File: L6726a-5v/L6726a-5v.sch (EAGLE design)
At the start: 32 parts, among them IC1 L6727A, U1 5V

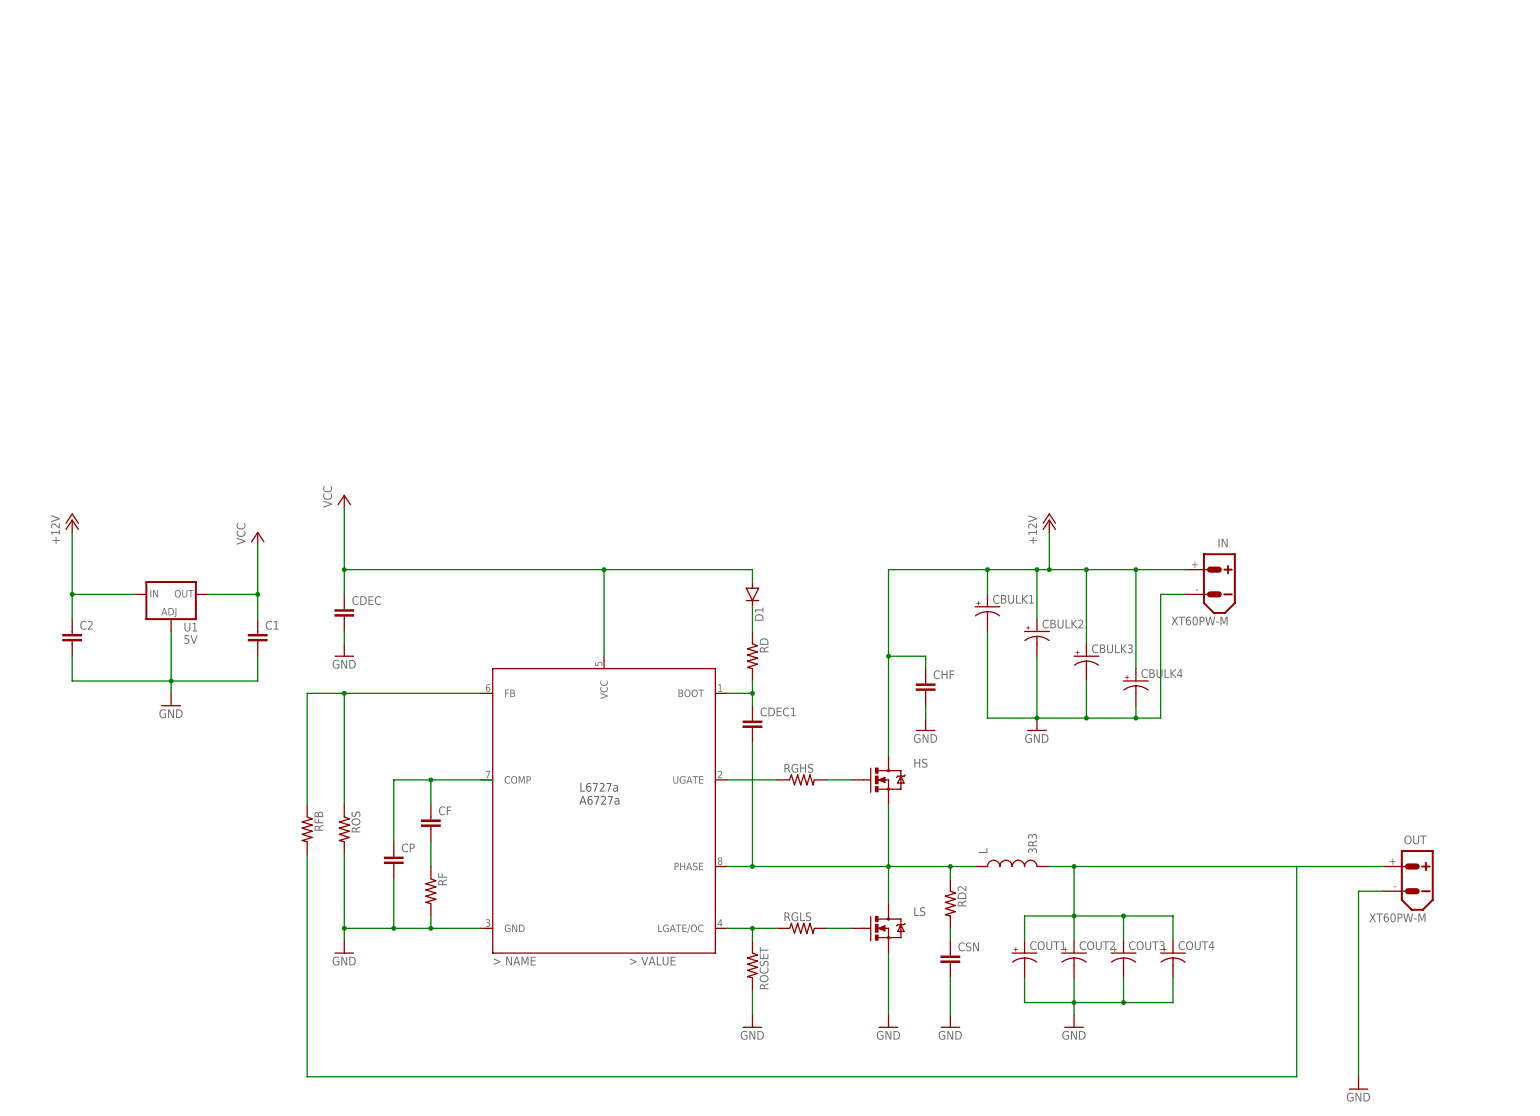
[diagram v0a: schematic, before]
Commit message: renamed files and folders, layout mostly complete
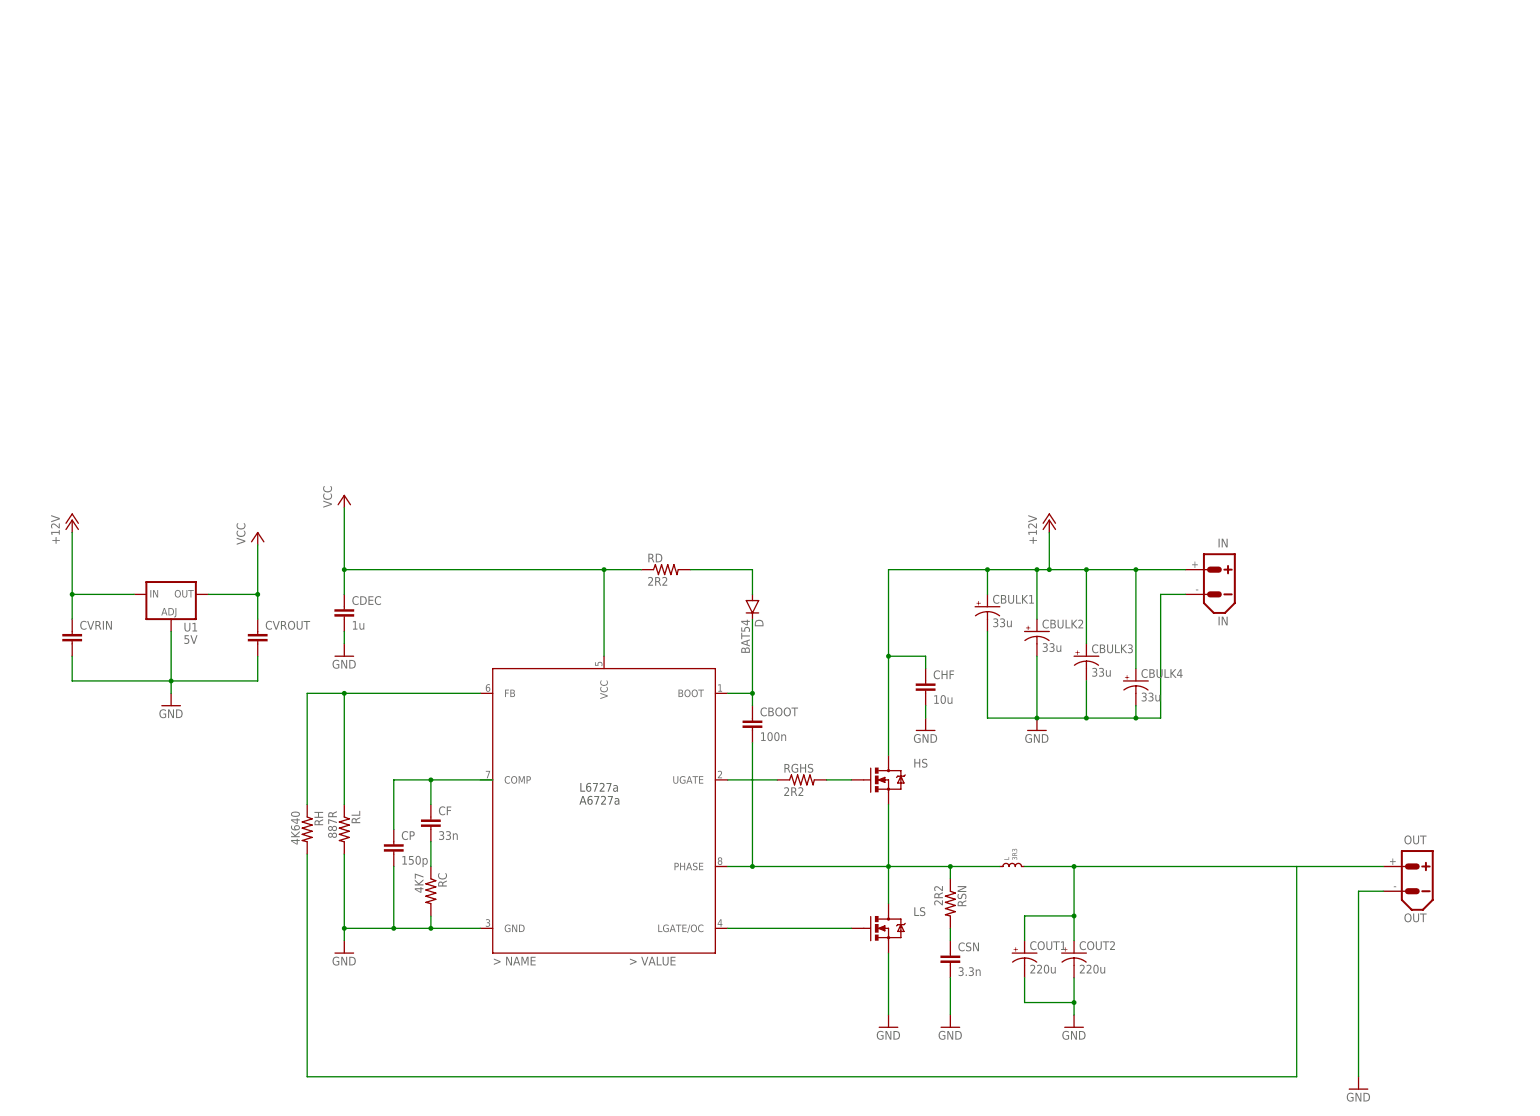
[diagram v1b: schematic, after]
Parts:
- removed CDEC1: (no value), rcl:C-EUC1206
- removed COUT3, COUT4: (no value), rcl:CPOL-USSANYO_SMD_E7
- removed D1: (no value), SparkFun-DiscreteSemi:DIODESOD123
- removed RGLS, ROCSET: (no value), rcl:R-US_R0603
- added CBOOT: 100n, rcl:C-EUC0805
- added D: BAT54, SparkFun-DiscreteSemi:DIODESOD123
- CBULK1, CBULK2, CBULK3, CBULK4: value (none) -> 33u
- CDEC: value (none) -> 1u; device rcl:C-EUC1206 -> rcl:C-EUC0603
- CF: value (none) -> 33n; device rcl:C-EUC1206 -> rcl:C-EUC0603
- CHF: value (none) -> 10u
- COUT1, COUT2: value (none) -> 220u
- CP: value (none) -> 150p; device rcl:C-EUC1206 -> rcl:C-EUC0603
- CSN: value (none) -> 3.3n; device rcl:C-EUC1206 -> rcl:C-EUC0603
- IN: value XT60PW-M -> IN
- L: device SparkFun-Passives:INDUCTORSDR13-7-270ML -> coilcraft:INDUCTOR.XAL1010
- OUT: value XT60PW-M -> OUT
- RC: value (none) -> 4K7
- RD, RGHS, RSN: value (none) -> 2R2
- RH: value (none) -> 4K640
- RL: value (none) -> 887R
- renumbered C1 to CVROUT, C2 to CVRIN, RD2 to RSN, RF to RC, RFB to RH, ROS to RL
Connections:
- removed net LGATE`: IC1.LGATE/OC, RGLS.1, ROCSET.1
- removed net N$2: CDEC1.1, IC1.BOOT, RD.2
- new net BOOT: CBOOT.1, D.C, IC1.BOOT
- net GND: no longer COUT3.-, COUT4.-, ROCSET.2
- net LGATE: now also IC1.LGATE/OC; no longer RGLS.2
- net N$1: now also D.A, RD.2; no longer D1.C, RD.1
- net PHASE: now also CBOOT.2; no longer CDEC1.2
- net VCC: now also RD.1; no longer D1.A
- net VOUT: no longer COUT3.+, COUT4.+
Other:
- moved on the sheet: CP, RD

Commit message: lots of progress with routing, verifying component packages
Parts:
- CBULK1, CBULK2, CBULK3, CBULK4: device rcl:CPOL-USSANYO_SMD_E7 -> rcl:C-EUC2220K
- COUT1, COUT2: value 220u -> 330u; device rcl:CPOL-USSANYO_SMD_E7 -> rcl:CPOL-USSANYO_SMD_C6
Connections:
- net +12V: now also CBULK1.1, CBULK2.1, CBULK3.1, CBULK4.1; no longer CBULK1.+, CBULK2.+, CBULK3.+, CBULK4.+
- net GND: now also CBULK1.2, CBULK2.2, CBULK3.2, CBULK4.2; no longer CBULK1.-, CBULK2.-, CBULK3.-, CBULK4.-
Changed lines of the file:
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@@
 <layer number="23" name="tOrigins" color="15" fill="1" visible="yes" active="no"/>
 <layer number="24" name="bOrigins" color="15" fill="1" visible="yes" active="no"/>
-<layer number="25" name="tNames" color="6" fill="1" visible="yes" active="no"/>
+<layer number="25" name="tNames" color="14" fill="1" visible="yes" active="no"/>
 <layer number="26" name="bNames" color="13" fill="1" visible="yes" active="no"/>
-<layer number="27" name="tValues" color="7" fill="1" visible="yes" active="no"/>
-<layer number="28" name="bValues" color="7" fill="1" visible="yes" active="no"/>
+<layer number="27" name="tValues" color="6" fill="1" visible="yes" active="no"/>
+<layer number="28" name="bValues" color="5" fill="1" visible="yes" active="no"/>
 <layer number="29" name="tStop" color="7" fill="3" visible="no" active="no"/>
 <layer number="30" name="bStop" color="7" fill="6" visible="no" active="no"/>
@@
 <part name="CSN" library="rcl" deviceset="C-EU" device="C0603" value="3.3n"/>
 <part name="RSN" library="rcl" deviceset="R-US_" device="R0603" value="2R2"/>
-<part name="CBULK1" library="rcl" deviceset="CPOL-US" device="SANYO_SMD_E7" value="33u"/>
-<part name="COUT1" library="rcl" deviceset="CPOL-US" device="SANYO_SMD_E7" value="220u"/>
-<part name="CBULK2" library="rcl" deviceset="CPOL-US" device="SANYO_SMD_E7" value="33u"/>
+<part name="COUT1" library="rcl" deviceset="CPOL-US" device="SANYO_SMD_C6" value="330u"/>
 <part name="GND8" library="supply1" deviceset="GND" device=""/>
-<part name="COUT2" library="rcl" deviceset="CPOL-US" device="SANYO_SMD_E7" value="220u"/>
+<part name="COUT2" library="rcl" deviceset="CPOL-US" device="SANYO_SMD_C6" value="330u"/>
 <part name="GND10" library="supply1" deviceset="GND" device=""/>
 <part name="GND4" library="supply1" deviceset="GND" device=""/>
@@
 <part name="OUT" library="amass" deviceset="XT60" device="PW-M" value="OUT"/>
 <part name="IN" library="amass" deviceset="XT60" device="PW-M" value="IN"/>
-<part name="CBULK3" library="rcl" deviceset="CPOL-US" device="SANYO_SMD_E7" value="33u"/>
-<part name="CBULK4" library="rcl" deviceset="CPOL-US" device="SANYO_SMD_E7" value="33u"/>
 <part name="L" library="coilcraft" deviceset="INDUCTOR" device=".XAL1010" value="3R3"/>
+<part name="CBULK1" library="rcl" deviceset="C-EU" device="C2220K" value="33u"/>
+<part name="CBULK2" library="rcl" deviceset="C-EU" device="C2220K" value="33u"/>
+<part name="CBULK3" library="rcl" deviceset="C-EU" device="C2220K" value="33u"/>
+<part name="CBULK4" library="rcl" deviceset="C-EU" device="C2220K" value="33u"/>
 </parts>
 <sheets>
@@
 <instance part="CSN" gate="G$1" x="149.86" y="10.16"/>
 <instance part="RSN" gate="G$1" x="149.86" y="20.32" rot="R270"/>
-<instance part="CBULK1" gate="G$1" x="157.48" y="81.28"/>
 <instance part="COUT1" gate="G$1" x="165.1" y="10.16"/>
-<instance part="CBULK2" gate="G$1" x="167.64" y="76.2"/>
 <instance part="GND8" gate="1" x="167.64" y="55.88"/>
 <instance part="COUT2" gate="G$1" x="175.26" y="10.16"/>
@@
 <instance part="OUT" gate="G$1" x="243.84" y="25.4" rot="MR0"/>
 <instance part="IN" gate="G$1" x="203.2" y="86.36" rot="MR0"/>
+<instance part="L" gate="G$1" x="162.56" y="27.94"/>
+<instance part="CBULK1" gate="G$1" x="157.48" y="81.28"/>
+<instance part="CBULK2" gate="G$1" x="167.64" y="76.2"/>
 <instance part="CBULK3" gate="G$1" x="177.8" y="71.12"/>
 <instance part="CBULK4" gate="G$1" x="187.96" y="66.04"/>
-<instance part="L" gate="G$1" x="162.56" y="27.94"/>
 </instances>
 <busses>
@@
 <wire x1="157.48" y1="83.82" x2="157.48" y2="88.9" width="0.1524" layer="91"/>
 <junction x="157.48" y="88.9"/>
-<pinref part="CBULK1" gate="G$1" pin="+"/>
-<pinref part="CBULK2" gate="G$1" pin="+"/>
 <wire x1="167.64" y1="88.9" x2="167.64" y2="78.74" width="0.1524" layer="91"/>
 <junction x="167.64" y="88.9"/>
@@
 <wire x1="198.12" y1="88.9" x2="187.96" y2="88.9" width="0.1524" layer="91"/>
 <junction x="177.8" y="88.9"/>
-<pinref part="CBULK3" gate="G$1" pin="+"/>
-<pinref part="CBULK4" gate="G$1" pin="+"/>
 <wire x1="187.96" y1="88.9" x2="177.8" y2="88.9" width="0.1524" layer="91"/>
 <wire x1="187.96" y1="68.58" x2="187.96" y2="88.9" width="0.1524" layer="91"/>
 <junction x="187.96" y="88.9"/>
+<pinref part="CBULK1" gate="G$1" pin="1"/>
+<pinref part="CBULK2" gate="G$1" pin="1"/>
+<pinref part="CBULK3" gate="G$1" pin="1"/>
+<pinref part="CBULK4" gate="G$1" pin="1"/>
 </segment>
 </net>
@@
 <segment>
 <pinref part="GND8" gate="1" pin="GND"/>
-<pinref part="CBULK2" gate="G$1" pin="-"/>
 <wire x1="167.64" y1="58.42" x2="167.64" y2="71.12" width="0.1524" layer="91"/>
 <wire x1="157.48" y1="58.42" x2="157.48" y2="76.2" width="0.1524" layer="91"/>
-<pinref part="CBULK1" gate="G$1" pin="-"/>
 <wire x1="157.48" y1="58.42" x2="167.64" y2="58.42" width="0.1524" layer="91"/>
 <junction x="167.64" y="58.42"/>
@@
 <wire x1="193.04" y1="58.42" x2="187.96" y2="58.42" width="0.1524" layer="91"/>
 <junction x="177.8" y="58.42"/>
-<pinref part="CBULK3" gate="G$1" pin="-"/>
-<pinref part="CBULK4" gate="G$1" pin="-"/>
 <wire x1="187.96" y1="58.42" x2="177.8" y2="58.42" width="0.1524" layer="91"/>
 <wire x1="187.96" y1="58.42" x2="187.96" y2="60.96" width="0.1524" layer="91"/>
 <junction x="187.96" y="58.42"/>
-</segment>
-<segment>
+<pinref part="CBULK1" gate="G$1" pin="2"/>
+<pinref part="CBULK2" gate="G$1" pin="2"/>
+<pinref part="CBULK3" gate="G$1" pin="2"/>
+<pinref part="CBULK4" gate="G$1" pin="2"/>
+</segment>
+<segment>

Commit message: changed mosfet package, blew up layout
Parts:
- CF: value 33n -> 15n
- CP: value 150p -> 22p
- HS, LS: value MOSFET-NCHANNELFDS6630A -> N_MOSFET_POWERSO8; device SparkFun-DiscreteSemi:MOSFET-NCHANNELFDS6630A -> power-mosfet:N_MOSFET_POWERSO8
- RC: value 4K7 -> 18K0
- RH, RL: device rcl:R-US_R0603 -> rcl:R-US_R0805
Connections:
- net N$3 renamed CC
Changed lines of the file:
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@@
 <part name="RGHS" library="rcl" deviceset="R-US_" device="R0603" value="2R2"/>
 <part name="CHF" library="rcl" deviceset="C-EU" device="C1206" value="10u"/>
-<part name="HS" library="SparkFun-DiscreteSemi" deviceset="MOSFET-NCHANNEL" device="FDS6630A" value=""/>
 <part name="P+4" library="supply1" deviceset="+12V" device=""/>
 <part name="GND3" library="supply1" deviceset="GND" device=""/>
-<part name="LS" library="SparkFun-DiscreteSemi" deviceset="MOSFET-NCHANNEL" device="FDS6630A" value=""/>
 <part name="GND5" library="supply1" deviceset="GND" device=""/>
 <part name="GND7" library="supply1" deviceset="GND" device=""/>
@@
 <part name="GND10" library="supply1" deviceset="GND" device=""/>
 <part name="GND4" library="supply1" deviceset="GND" device=""/>
-<part name="RH" library="rcl" deviceset="R-US_" device="R0603" value="4K640"/>
-<part name="RL" library="rcl" deviceset="R-US_" device="R0603" value="887R"/>
-<part name="CP" library="rcl" deviceset="C-EU" device="C0603" value="150p"/>
-<part name="CF" library="rcl" deviceset="C-EU" device="C0603" value="33n"/>
-<part name="RC" library="rcl" deviceset="R-US_" device="R0603" value="4K7"/>
+<part name="RH" library="rcl" deviceset="R-US_" device="R0805" value="4K640"/>
+<part name="RL" library="rcl" deviceset="R-US_" device="R0805" value="887R"/>
+<part name="CP" library="rcl" deviceset="C-EU" device="C0603" value="22p"/>
+<part name="CF" library="rcl" deviceset="C-EU" device="C0603" value="15n"/>
+<part name="RC" library="rcl" deviceset="R-US_" device="R0603" value="18K0"/>
 <part name="GND9" library="supply1" deviceset="GND" device=""/>
 <part name="OUT" library="amass" deviceset="XT60" device="PW-M" value="OUT"/>
@@
 <part name="CBULK3" library="rcl" deviceset="C-EU" device="C2220K" value="33u"/>
 <part name="CBULK4" library="rcl" deviceset="C-EU" device="C2220K" value="33u"/>
+<part name="HS" library="power-mosfet" deviceset="N_MOSFET_POWERSO8" device="" value=""/>
+<part name="LS" library="power-mosfet" deviceset="N_MOSFET_POWERSO8" device="" value=""/>
 </parts>
 <sheets>
@@
 <instance part="RGHS" gate="G$1" x="119.38" y="45.72"/>
 <instance part="CHF" gate="G$1" x="144.78" y="66.04"/>
-<instance part="HS" gate="G$1" x="137.16" y="45.72"/>
 <instance part="P+4" gate="1" x="170.18" y="99.06"/>
 <instance part="GND3" gate="1" x="144.78" y="55.88"/>
-<instance part="LS" gate="G$1" x="137.16" y="15.24"/>
 <instance part="GND5" gate="1" x="149.86" y="-5.08"/>
 <instance part="GND7" gate="1" x="137.16" y="-5.08"/>
@@
 <instance part="CBULK3" gate="G$1" x="177.8" y="71.12"/>
 <instance part="CBULK4" gate="G$1" x="187.96" y="66.04"/>
+<instance part="HS" gate="G$1" x="134.62" y="48.26"/>
+<instance part="LS" gate="G$1" x="134.62" y="17.78"/>
 </instances>
 <busses>
@@
 <pinref part="P+4" gate="1" pin="+12V"/>
 <wire x1="170.18" y1="96.52" x2="170.18" y2="88.9" width="0.1524" layer="91"/>
-<pinref part="HS" gate="G$1" pin="D"/>
 <wire x1="170.18" y1="88.9" x2="167.64" y2="88.9" width="0.1524" layer="91"/>
 <wire x1="167.64" y1="88.9" x2="157.48" y2="88.9" width="0.1524" layer="91"/>
@@
 <wire x1="137.16" y1="88.9" x2="137.16" y2="71.12" width="0.1524" layer="91"/>
 <pinref part="CHF" gate="G$1" pin="1"/>
-<wire x1="137.16" y1="71.12" x2="137.16" y2="50.8" width="0.1524" layer="91"/>
+<wire x1="137.16" y1="71.12" x2="137.16" y2="53.34" width="0.1524" layer="91"/>
 <wire x1="144.78" y1="68.58" x2="144.78" y2="71.12" width="0.1524" layer="91"/>
 <wire x1="144.78" y1="71.12" x2="137.16" y2="71.12" width="0.1524" layer="91"/>
@@
 <pinref part="CBULK3" gate="G$1" pin="1"/>
 <pinref part="CBULK4" gate="G$1" pin="1"/>
+<pinref part="HS" gate="G$1" pin="D"/>
 </segment>
 </net>
@@
 <segment>
 <pinref part="GND7" gate="1" pin="GND"/>
+<wire x1="137.16" y1="-2.54" x2="137.16" y2="12.7" width="0.1524" layer="91"/>
 <pinref part="LS" gate="G$1" pin="S"/>
-<wire x1="137.16" y1="-2.54" x2="137.16" y2="10.16" width="0.1524" layer="91"/>
 </segment>
 <segment>
@@
 <segment>
 <pinref part="RGHS" gate="G$1" pin="2"/>
+<wire x1="124.46" y1="45.72" x2="132.08" y2="45.72" width="0.1524" layer="91"/>
 <pinref part="HS" gate="G$1" pin="G"/>
-<wire x1="124.46" y1="45.72" x2="129.54" y2="45.72" width="0.1524" layer="91"/>
 </segment>
 </net>
@@
 </segment>
 </net>
-<net name="N$3" class="0">
+<net name="CC" class="0">
 <segment>
 <pinref part="RC" gate="G$1" pin="1"/>
@@
 <pinref part="RSN" gate="G$1" pin="1"/>
 <wire x1="149.86" y1="25.4" x2="149.86" y2="27.94" width="0.1524" layer="91"/>
-<pinref part="HS" gate="G$1" pin="S"/>
-<pinref part="LS" gate="G$1" pin="D"/>
-<wire x1="137.16" y1="20.32" x2="137.16" y2="27.94" width="0.1524" layer="91"/>
-<wire x1="137.16" y1="27.94" x2="137.16" y2="40.64" width="0.1524" layer="91"/>
+<wire x1="137.16" y1="22.86" x2="137.16" y2="27.94" width="0.1524" layer="91"/>
+<wire x1="137.16" y1="27.94" x2="137.16" y2="43.18" width="0.1524" layer="91"/>
 <junction x="137.16" y="27.94"/>
 <wire x1="137.16" y1="27.94" x2="149.86" y2="27.94" width="0.1524" layer="91"/>
@@
 <junction x="149.86" y="27.94"/>
 <pinref part="L" gate="G$1" pin="1"/>
+<pinref part="HS" gate="G$1" pin="S"/>
+<pinref part="LS" gate="G$1" pin="D"/>
 </segment>
 </net>
@@
 <segment>
 <pinref part="IC1" gate="G$1" pin="LGATE/OC"/>
+<wire x1="104.14" y1="15.24" x2="132.08" y2="15.24" width="0.1524" layer="91"/>
 <pinref part="LS" gate="G$1" pin="G"/>
-<wire x1="104.14" y1="15.24" x2="129.54" y2="15.24" width="0.1524" layer="91"/>
-</segment>
-</net>
+</segment>
+</net>

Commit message: finished routing transistors, still need LDO
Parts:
- RGHS: device rcl:R-US_R0603 -> rcl:R-US_R0805
- renumbered CF to CC
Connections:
- net COMP: now also IC1.COMP
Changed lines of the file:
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@@
 <part name="D" library="SparkFun-DiscreteSemi" deviceset="DIODE" device="SOD123" value="BAT54"/>
 <part name="CBOOT" library="rcl" deviceset="C-EU" device="C0805" value="100n"/>
-<part name="RGHS" library="rcl" deviceset="R-US_" device="R0603" value="2R2"/>
+<part name="RGHS" library="rcl" deviceset="R-US_" device="R0805" value="2R2"/>
 <part name="CHF" library="rcl" deviceset="C-EU" device="C1206" value="10u"/>
 <part name="P+4" library="supply1" deviceset="+12V" device=""/>
@@
 <part name="RL" library="rcl" deviceset="R-US_" device="R0805" value="887R"/>
 <part name="CP" library="rcl" deviceset="C-EU" device="C0603" value="22p"/>
-<part name="CF" library="rcl" deviceset="C-EU" device="C0603" value="15n"/>
+<part name="CC" library="rcl" deviceset="C-EU" device="C0603" value="15n"/>
 <part name="RC" library="rcl" deviceset="R-US_" device="R0603" value="18K0"/>
 <part name="GND9" library="supply1" deviceset="GND" device=""/>
@@
 <instance part="RL" gate="G$1" x="25.4" y="35.56" rot="R270"/>
 <instance part="CP" gate="G$1" x="35.56" y="33.02"/>
-<instance part="CF" gate="G$1" x="43.18" y="38.1"/>
+<instance part="CC" gate="G$1" x="43.18" y="38.1"/>
 <instance part="RC" gate="G$1" x="43.18" y="22.86" rot="R270"/>
 <instance part="GND9" gate="1" x="233.68" y="-17.78"/>
@@
 <net name="COMP" class="0">
 <segment>
-<wire x1="55.88" y1="45.72" x2="43.18" y2="45.72" width="0.1524" layer="91"/>
 <wire x1="43.18" y1="45.72" x2="35.56" y2="45.72" width="0.1524" layer="91"/>
 <wire x1="35.56" y1="45.72" x2="35.56" y2="35.56" width="0.1524" layer="91"/>
-<pinref part="CF" gate="G$1" pin="1"/>
+<pinref part="CC" gate="G$1" pin="1"/>
 <wire x1="43.18" y1="40.64" x2="43.18" y2="45.72" width="0.1524" layer="91"/>
+<pinref part="CP" gate="G$1" pin="1"/>
+<pinref part="IC1" gate="G$1" pin="COMP"/>
+<wire x1="43.18" y1="45.72" x2="53.34" y2="45.72" width="0.1524" layer="91"/>
 <junction x="43.18" y="45.72"/>
-<pinref part="CP" gate="G$1" pin="1"/>
 </segment>
 </net>
@@
 <segment>
 <pinref part="RC" gate="G$1" pin="1"/>
-<pinref part="CF" gate="G$1" pin="2"/>
+<pinref part="CC" gate="G$1" pin="2"/>
 <wire x1="43.18" y1="27.94" x2="43.18" y2="33.02" width="0.1524" layer="91"/>
 </segment>
